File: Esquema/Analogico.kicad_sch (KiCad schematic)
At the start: 33 parts, among them J1 Conex_bat, J2 Conn_01x02, J3 Galga_1, J4 Galga_2, J5 Conn_01x02, P1 USB_C_Plug_USB2.0, U1 REF3020AIDBZT, U2 TMUX154EDGS, U3 TP4057, U4 INA826AIDR, U5 INA826AIDR, U6 XL006, U7 TLV75733PDBV, U8 TLV75733PDBV

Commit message: Cambios en el esquematico del viernes
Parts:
- removed D2: D_Schottky, symbol Device:D_Schottky
- added C4: 47u, Capacitor_SMD:C_0805_2012Metric, symbol Device:C
- added D3: 1N5822, Diode_THT:D_DO-201AD_P15.24mm_Horizontal, symbol Diode:1N5822
- C3: value C -> 220u; footprint (none) -> Capacitor_SMD:C_1206_3216Metric
- C3: value C -> 220u
- L1, L2: value L -> 33u; footprint (none) -> Inductor_SMD:L_APV_APH0630; JLC (none) -> C5349704
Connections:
- net GND: now also C4.2
- net at C3.1, D1.1 (K), P1.A4 (VBUS)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: now also D3.1 (K)
- net at J2.2 (Pin_2), L1.1, U6.2 (EN)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: now also C4.1
- net at C3.2, L2.2: now also D3.2 (A)
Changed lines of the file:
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@@
 		)
 	)
-	(text_box "Mirar datasheet para ver valores"
-		(exclude_from_sim no)
-		(at 17.78 17.78 0)
-		(size 104.14 41.91)
-		(margins 0.9525 0.9525 0.9525 0.9525)
-		(stroke
-			(width 0)
-			(type solid)
-		)
-		(fill
-			(type none)
-		)
-		(effects
-			(font
-				(size 1.27 1.27)
-			)
-			(justify left top)
-		)
-	)
 	(text_box "Mirar datasheet del peso\n"
 		(exclude_from_sim no)
@@
 		(color 0 0 0 0)
 	)
+	(junction
+		(at 39.37 31.75)
+		(diameter 0)
+		(color 0 0 0 0)
+	)
 	(no_connect
 		(at 68.58 66.04)
@@
 	(wire
 		(pts
-			(xy 34.29 31.75) (xy 43.18 31.75)
+			(xy 34.29 31.75) (xy 39.37 31.75)
 		)
 		(stroke
@@
 	(wire
 		(pts
+			(xy 39.37 31.75) (xy 43.18 31.75)
+		)
+		(stroke
+			(width 0)
+			(type default)
+		)
+	)
+	(wire
+		(pts
 			(xy 160.02 48.26) (xy 166.37 48.26)
 		)
@@
 			)
 		)
-		(property "Value" "L"
+		(property "Value" "33u"
 			(at 54.61 22.86 90)
 			(effects
@@
 			)
 		)
-		(property "Footprint" ""
+		(property "Footprint" "Inductor_SMD:L_APV_APH0630"
 			(at 54.61 25.4 0)
 			(effects
@@
 			)
 		)
+		(property "JLC" "C5349704"
+			(at 54.61 25.4 90)
+			(effects
+				(font
+					(size 1.27 1.27)
+				)
+				(hide yes)
+			)
+		)
 		(pin "1"
 		)
@@
 	)
 	(symbol
+		(lib_id "Diode:1N5822")
+		(at 87.63 31.75 180)
+		(unit 1)
+		(exclude_from_sim no)
+		(in_bom yes)
+		(on_board yes)
+		(dnp no)
+		(fields_autoplaced yes)
+		(property "Reference" "D3"
+			(at 87.9475 25.4 0)
+			(effects
+				(font
+					(size 1.27 1.27)
+				)
+			)
+		)
+		(property "Value" "1N5822"
+			(at 87.9475 27.94 0)
+			(effects
+				(font
+					(size 1.27 1.27)
+				)
+			)
+		)
+		(property "Footprint" "Diode_THT:D_DO-201AD_P15.24mm_Horizontal"
+			(at 87.63 27.305 0)
+			(effects
+				(font
+					(size 1.27 1.27)
+				)
+				(hide yes)
+			)
+		)
+		(property "Datasheet" "http://www.vishay.com/docs/88526/1n5820.pdf"
+			(at 87.63 31.75 0)
+			(effects
+				(font
+					(size 1.27 1.27)
+				)
+				(hide yes)
+			)
+		)
+		(property "Description" "40V 3A Schottky Barrier Rectifier Diode, DO-201AD"
+			(at 87.63 31.75 0)
+			(effects
+				(font
+					(size 1.27 1.27)
+				)
+				(hide yes)
+			)
+		)
+		(property "JLC" "C2476"
+			(at 87.63 31.75 0)
+			(effects
+				(font
+					(size 1.27 1.27)
+				)
+				(hide yes)
+			)
+		)
+		(pin "2"
+		)
+		(pin "1"
+		)
+		(instances
+			(project ""
+				(path "/c0191433-e910-4547-8328-ff407e20805d"
+					(reference "D3")
+					(unit 1)
+				)
+			)
+		)
+	)
+	(symbol
 		(lib_id "Device:C")
 		(at 110.49 35.56 0)
@@
 			)
 		)
-		(property "Value" "C"
+		(property "Value" "220u"
 			(at 114.3 36.8299 0)
 			(effects
@@
 			)
 		)
-		(property "Footprint" ""
+		(property "Footprint" "Capacitor_SMD:C_1206_3216Metric"
 			(at 111.4552 39.37 0)
 			(effects
@@
 	)
 	(symbol
-		(lib_id "Device:D_Schottky")
-		(at 87.63 31.75 180)
-		(unit 1)
-		(exclude_from_sim no)
-		(in_bom yes)
-		(on_board yes)
-		(dnp no)
-		(fields_autoplaced yes)
-		(property "Reference" "D2"
-			(at 87.9475 25.4 0)
-			(effects
-				(font
-					(size 1.27 1.27)
-				)
-			)
-		)
-		(property "Value" "D_Schottky"
-			(at 87.9475 27.94 0)
-			(effects
-				(font
-					(size 1.27 1.27)
-				)
-			)
-		)
-		(property "Footprint" ""
-			(at 87.63 31.75 0)
-			(effects
-				(font
-					(size 1.27 1.27)
-				)
-				(hide yes)
-			)
-		)
-		(property "Datasheet" "~"
-			(at 87.63 31.75 0)
-			(effects
-				(font
-					(size 1.27 1.27)
-				)
-				(hide yes)
-			)
-		)
-		(property "Description" "Schottky diode"
-			(at 87.63 31.75 0)
-			(effects
-				(font
-					(size 1.27 1.27)
-				)
-				(hide yes)
-			)
-		)
-		(pin "1"
-		)
-		(pin "2"
-		)
-		(instances
-			(project "Analogico"
-				(path "/c0191433-e910-4547-8328-ff407e20805d"
-					(reference "D2")
-					(unit 1)
-				)
-			)
-		)
-	)
-	(symbol
 		(lib_id "power:GND")
 		(at 179.07 43.18 90)
@@
 			)
 		)
-		(property "Value" "C"
+		(property "Value" "220u"
 			(at 73.66 26.67 90)
 			(effects
@@
 	)
 	(symbol
+		(lib_id "Device:C")
+		(at 39.37 35.56 0)
+		(unit 1)
+		(exclude_from_sim no)
+		(in_bom yes)
+		(on_board yes)
+		(dnp no)
+		(property "Reference" "C4"
+			(at 43.18 34.2899 0)
+			(effects
+				(font
+					(size 1.27 1.27)
+				)
+				(justify left)
+			)
+		)
+		(property "Value" "47u"
+			(at 41.656 39.116 0)
+			(effects
+				(font
+					(size 1.27 1.27)
+				)
+				(justify left)
+			)
+		)
+		(property "Footprint" "Capacitor_SMD:C_0805_2012Metric"
+			(at 40.3352 39.37 0)
+			(effects
+				(font
+					(size 1.27 1.27)
+				)
+				(hide yes)
+			)
+		)
+		(property "Datasheet" "~"
+			(at 39.37 35.56 0)
+			(effects
+				(font
+					(size 1.27 1.27)
+				)
+				(hide yes)
+			)
+		)
+		(property "Description" "Unpolarized capacitor"
+			(at 39.37 35.56 0)
+			(effects
+				(font
+					(size 1.27 1.27)
+				)
+				(hide yes)
+			)
+		)
+		(property "JLC" "C16780"
+			(at 39.37 35.56 0)
+			(effects
+				(font
+					(size 1.27 1.27)
+				)
+				(hide yes)
+			)
+		)
+		(pin "1"
+		)
+		(pin "2"
+		)
+		(instances
+			(project "Analogico"
+				(path "/c0191433-e910-4547-8328-ff407e20805d"
+					(reference "C4")
+					(unit 1)
+				)
+			)
+		)
+	)
+	(symbol
+		(lib_id "power:GND")
+		(at 39.37 39.37 0)
+		(unit 1)
+		(exclude_from_sim no)
+		(in_bom yes)
+		(on_board yes)
+		(dnp no)
+		(fields_autoplaced yes)
+		(property "Reference" "#PWR024"
+			(at 39.37 45.72 0)
+			(effects
+				(font
+					(size 1.27 1.27)
+				)
+				(hide yes)
+			)
+		)
+		(property "Value" "GND"
+			(at 39.37 44.45 0)
+			(effects
+				(font
+					(size 1.27 1.27)
+				)
+			)
+		)
+		(property "Footprint" ""
+			(at 39.37 39.37 0)
+			(effects
+				(font
+					(size 1.27 1.27)
+				)
+				(hide yes)
+			)
+		)
+		(property "Datasheet" ""
+			(at 39.37 39.37 0)
+			(effects
+				(font
+					(size 1.27 1.27)
+				)
+				(hide yes)
+			)
+		)
+		(property "Description" "Power symbol creates a global label with name \"GND\" , ground"
+			(at 39.37 39.37 0)
+			(effects
+				(font
+					(size 1.27 1.27)
+				)
+				(hide yes)
+			)
+		)
+		(pin "1"
+		)
+		(instances
+			(project "Analogico"
+				(path "/c0191433-e910-4547-8328-ff407e20805d"
+					(reference "#PWR024")
+					(unit 1)
+				)
+			)
+		)
+	)
+	(symbol
 		(lib_id "libreria_proy:XL6008")
 		(at 54.61 34.29 0)
@@
 			)
 		)
-		(property "Value" "L"
+		(property "Value" "33u"
 			(at 82.55 39.3699 0)
 			(effects
@@
 			)
 		)
-		(property "Footprint" ""
+		(property "Footprint" "Inductor_SMD:L_APV_APH0630"
 			(at 81.28 38.1 0)
 			(effects
@@
 			(at 81.28 38.1 0)
 			(effects
+				(font
+					(size 1.27 1.27)
+				)
+				(hide yes)
+			)
+		)
+		(property "JLC" "C5349704"
+			(at 81.28 38.1 0)
+			(effects

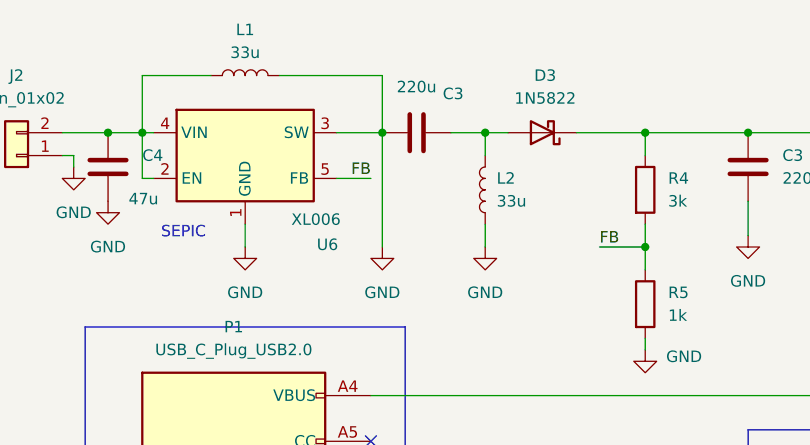
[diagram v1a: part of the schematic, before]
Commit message: He añadido los correspondientes datasheets y he corregido un componente que estaba mal colocado.
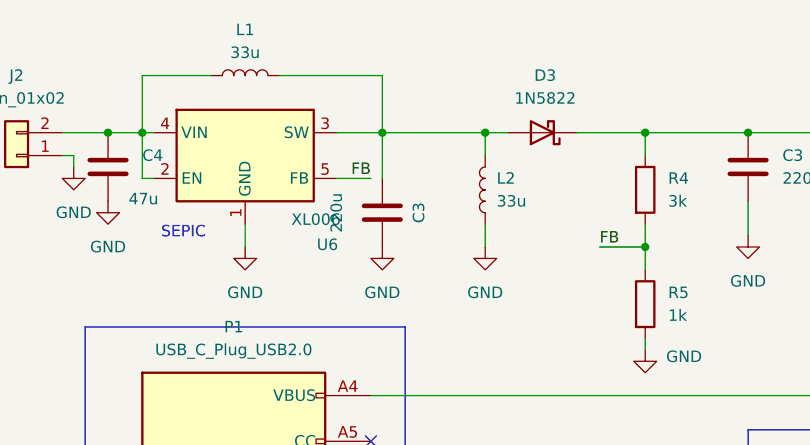
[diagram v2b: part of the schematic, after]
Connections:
- net GND: no longer L1.2, U6.3 (SW)
- net at C3.2, D3.2 (A), L2.2: now also L1.2, U6.3 (SW)
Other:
- moved on the sheet: C3
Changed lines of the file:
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@@
 	)
 	(junction
-		(at 125.73 60.96)
+		(at 69.85 31.75)
 		(diameter 0)
 		(color 0 0 0 0)
 	)
 	(junction
-		(at 69.85 31.75)
+		(at 125.73 60.96)
 		(diameter 0)
 		(color 0 0 0 0)
@@
 	(wire
 		(pts
-			(xy 69.85 44.45) (xy 69.85 31.75)
+			(xy 166.37 71.12) (xy 185.42 71.12)
 		)
 		(stroke
@@
 	(wire
 		(pts
-			(xy 166.37 71.12) (xy 185.42 71.12)
+			(xy 99.06 44.45) (xy 99.06 46.99)
 		)
 		(stroke
@@
 	(wire
 		(pts
-			(xy 99.06 44.45) (xy 99.06 46.99)
+			(xy 76.2 137.16) (xy 78.74 137.16)
 		)
 		(stroke
@@
 	(wire
 		(pts
-			(xy 76.2 137.16) (xy 78.74 137.16)
+			(xy 69.85 31.75) (xy 69.85 36.83)
 		)
 		(stroke
@@
 	(wire
 		(pts
+			(xy 69.85 31.75) (xy 81.28 31.75)
+		)
+		(stroke
+			(width 0)
+			(type default)
+		)
+	)
+	(wire
+		(pts
 			(xy 87.63 144.78) (xy 87.63 137.16)
 		)
@@
 	(wire
 		(pts
-			(xy 77.47 31.75) (xy 81.28 31.75)
-		)
-		(stroke
-			(width 0)
-			(type default)
-		)
-	)
-	(wire
-		(pts
 			(xy 248.92 92.71) (xy 248.92 93.98)
 		)
@@
 			)
 		)
-		(property "Datasheet" "~"
+		(property "Datasheet" "https://www.lcsc.com/datasheet/C5349704.pdf"
 			(at 54.61 25.4 0)
 			(effects
@@
 	(symbol
 		(lib_id "Device:C")
-		(at 73.66 31.75 90)
+		(at 69.85 40.64 180)
 		(unit 1)
 		(exclude_from_sim no)
@@
 		(dnp no)
 		(property "Reference" "C3"
-			(at 77.724 27.432 90)
+			(at 73.914 40.64 90)
 			(effects
 				(font
@@
 		)
 		(property "Value" "220u"
-			(at 73.66 26.67 90)
+			(at 64.77 40.64 90)
 			(effects
 				(font
@@
 		)
 		(property "Footprint" ""
-			(at 77.47 30.7848 0)
+			(at 68.8848 36.83 0)
 			(effects
 				(font
@@
 		)
 		(property "Datasheet" "~"
-			(at 73.66 31.75 0)
+			(at 69.85 40.64 0)
 			(effects
 				(font
@@
 		)
 		(property "Description" "Unpolarized capacitor"
-			(at 73.66 31.75 0)
+			(at 69.85 40.64 0)
 			(effects
 				(font
@@
 			)
 		)
-		(property "Datasheet" "~"
+		(property "Datasheet" "https://www.lcsc.com/datasheet/C5349704.pdf"
 			(at 81.28 38.1 0)
 			(effects

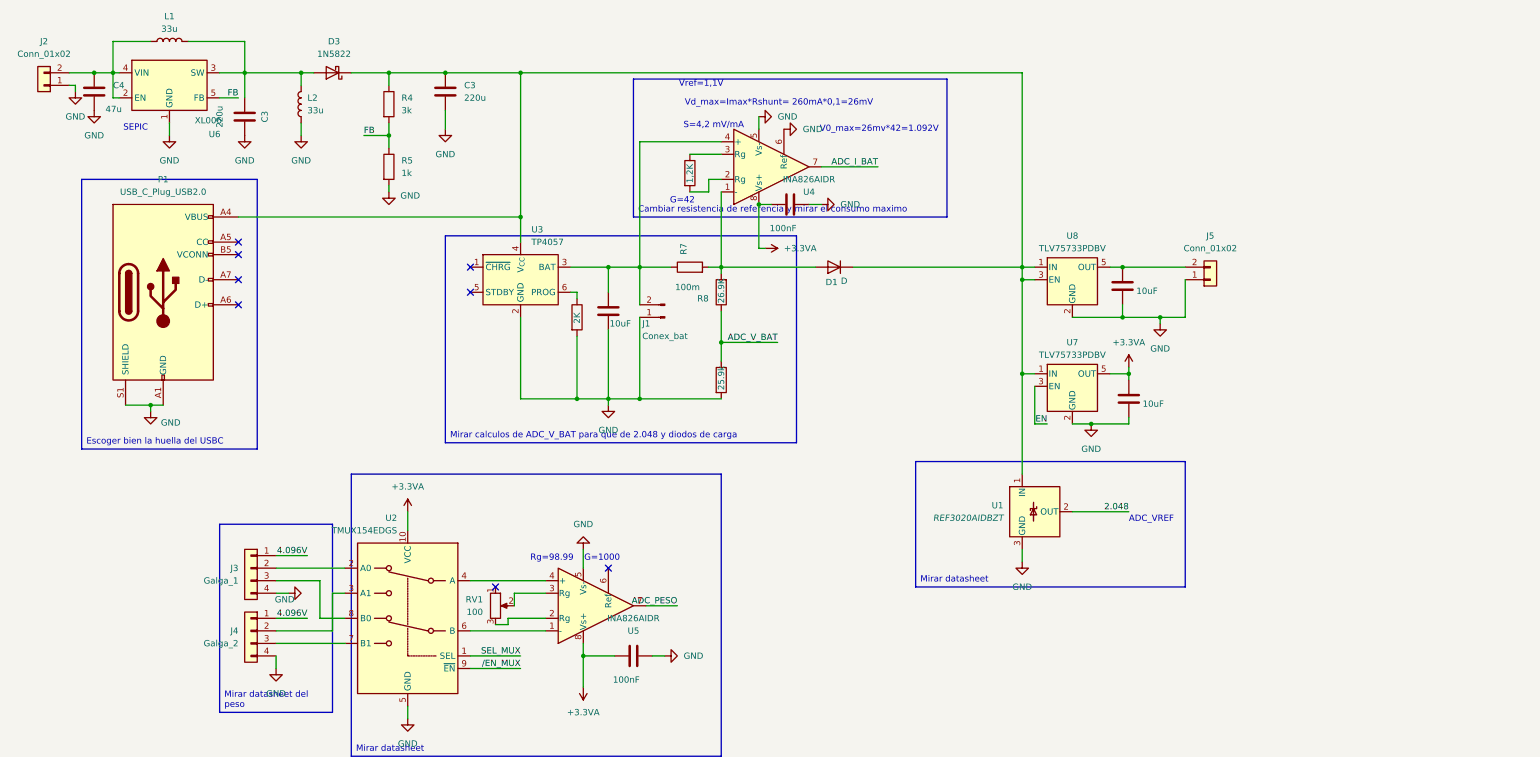
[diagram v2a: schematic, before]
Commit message: He añadido la footprint y simbolo del stm32f429zi
Signed-off-by: ricardo.socorro <ricardo.socorro@alumnos.upm.es>
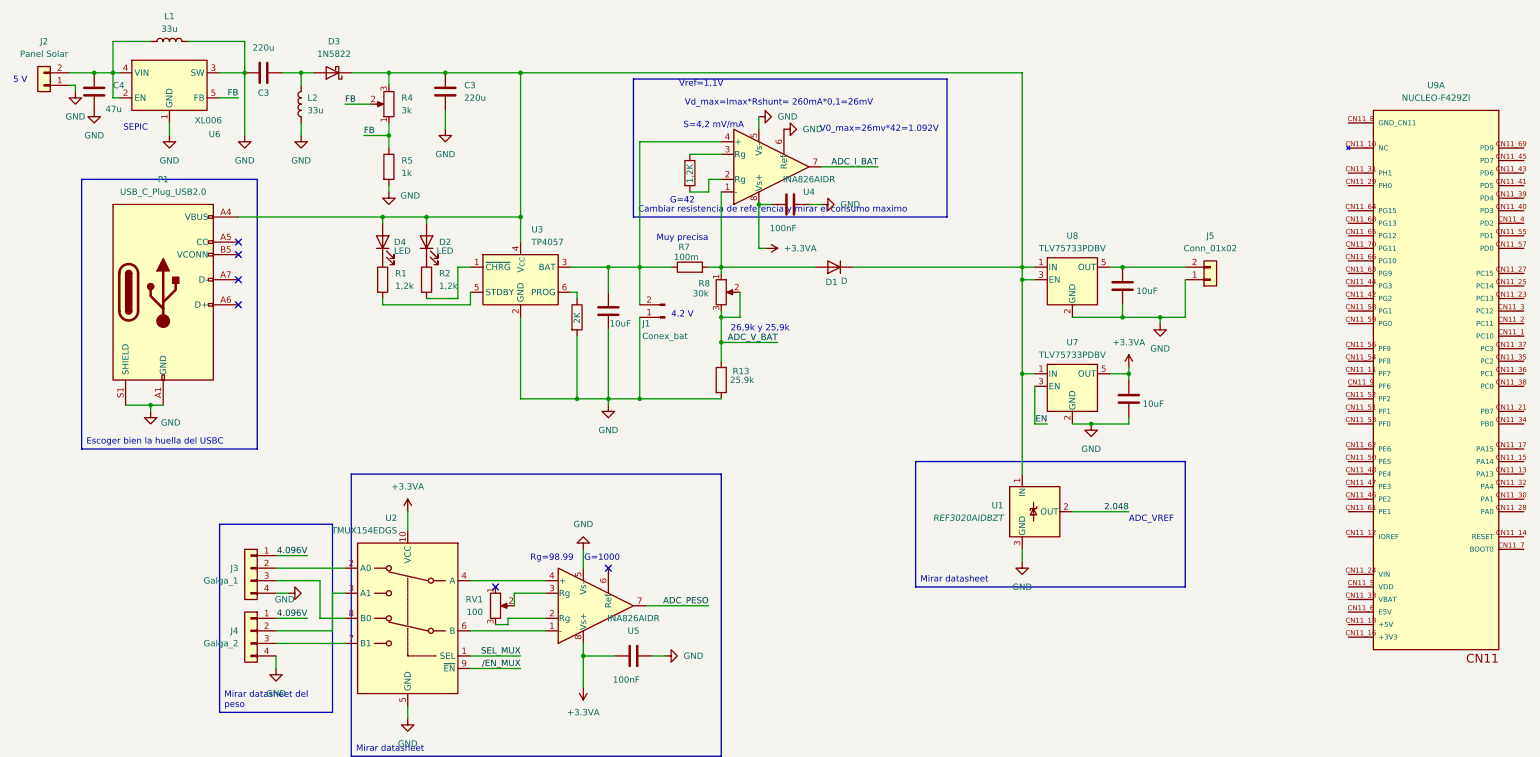
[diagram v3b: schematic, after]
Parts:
- removed R4: 3k, symbol Device:R
- removed R8: 26.9K, Resistor_SMD:R_0603_1608Metric, symbol Device:R
- added D2, D4: LED, symbol Device:LED
- added R1, R2: 1,2k, symbol Device:R
- added R4: 3k, symbol Device:R_Potentiometer
- added R8: 30k, symbol Device:R_Potentiometer
- added U9: NUCLEO-F429ZI, stm32f429zi_symbol_footprint:MODULE_NUCLEO-F429ZI, symbol NUCLEO-F429ZI:NUCLEO-F429ZI
- J2: value Conn_01x02 -> Panel Solar
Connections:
- net ADC_V_BAT: now also R8.2, R8.3
- net FB: now also R4.1, R4.2
- net GND: now also L1.2, U6.3 (SW)
- net at D1.2 (A), R7.2, U4.1 (-): now also R8.1
- net at C3.1, D1.1 (K), D3.1 (K)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: now also D2.2 (A), D4.2 (A), R4.3
- net at C3.2, D3.2 (A), L2.2: no longer L1.2, U6.3 (SW)
- net at U3.1 (~{CHRG}): now also R2.2
- net at U3.5 (STDBY): now also R1.2
- new net: D2.1 (K), R2.1
- new net: D4.1 (K), R1.1
- new net: U9.CN11_10 (NC), U9.CN11_26 (NC), U9.CN11_67 (NC)
- new net GND_CN11: U9.CN11_19 (GND_CN11), U9.CN11_20 (GND_CN11), U9.CN11_22 (GND_CN11), U9.CN11_49 (GND_CN11), U9.CN11_60 (GND_CN11), U9.CN11_71 (GND_CN11), U9.CN11_72 (GND_CN11), U9.CN11_8 (GND_CN11)
- no-connect marks 8 -> 6
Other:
- note added: "26,9k y 25,9k"
- note added: "4.2 V"
- note added: "5 V"
- note added: "Muy precisa"
- moved on the sheet: C3

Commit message: Huellas y componentes ya asignados
Signed-off-by: ricardo.socorro <ricardo.socorro@alumnos.upm.es>
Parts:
- added C6: 470nF, Capacitor_SMD:C_0805_2012Metric, symbol Device:C
- added R3: 1.5k, Resistor_SMD:R_0805_2012Metric, symbol Device:R
- added R9: 26.1k, Resistor_SMD:R_0805_2012Metric, symbol Device:R
- C10: renamed from C3; value 220u -> 220uF; footprint (none) -> Capacitor_SMD:C_1206_3216Metric; JLC (none) -> C412252
- C4: value 47u -> 47uF
- C9: renamed from C3; value 220u -> 220uF; JLC (none) -> C412252
- D2, D4: footprint (none) -> LED_THT:LED_D3.0mm; JLC (none) -> C85161
- J1: footprint (none) -> Connector_JST:JST_PH_S2B-PH-K_1x02_P2.00mm_Horizontal
- J2, J3, J4, J5: footprint (none) -> TerminalBlock_4Ucon:TerminalBlock_4Ucon_1x02_P3.50mm_Horizontal; JLC (none) -> C695629
- P1: footprint (none) -> Connector_USB:USB_C_Plug_ShenzhenJingTuoJin_918-118A2021Y40002_Vertical
- R1, R2: footprint (none) -> Resistor_SMD:R_0805_2012Metric; JLC (none) -> C114526
- R13: value 25.9k -> 25.5k
- R4: value 3k -> 2k; footprint (none) -> Potentiometer_THT:Potentiometer_Bourns_3266Y_Vertical; JLC (none) -> C48997938
- R5: footprint (none) -> Resistor_SMD:R_0805_2012Metric
- R8: value 30k -> 1k; footprint (none) -> Potentiometer_THT:Potentiometer_Bourns_3266Y_Vertical; JLC (none) -> C48997938
- RV1: footprint (none) -> Potentiometer_THT:Potentiometer_Bourns_3266Y_Vertical; JLC (none) -> C48997939
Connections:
- net FB: now also R3.2; no longer R4.1, R4.2
- net GND: now also C6.2
- net at D1.2 (A), R7.2, U4.1 (-): now also R9.1; no longer R8.1
- net at C9.1, D1.1 (K), D2.2 (A)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: now also R4.2, C6.1
- new net: R3.1, R4.1
- new net: R8.1, R9.2
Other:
- note added: "26,9k y 25,9k y 1%"
- note added: "3k y 1k"
- note added: "No existe 25.9k Usamos 25.5k y la de arriba tiene que ser menos de 26.5k"
- note removed: "26,9k y 25,9k"
- moved on the sheet: R13, R4, R5, R8, U9A

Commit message: PCB 1.0
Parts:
- removed J5: Conn_01x02, TerminalBlock_4Ucon:TerminalBlock_4Ucon_1x02_P3.50mm_Horizontal, symbol Connector_Generic:Conn_01x02
- removed U2: TMUX154EDGS, Package_SO:VSSOP-10_3x3mm_P0.5mm, symbol Analog_Switch:TMUX154EDGS
- removed U9: NUCLEO-F429ZI, stm32f429zi_symbol_footprint:MODULE_NUCLEO-F429ZI, symbol NUCLEO-F429ZI:NUCLEO-F429ZI
- added C3: 100nF, Capacitor_SMD:C_0805_2012Metric, symbol Device:C
- added RV2: 100, Potentiometer_THT:Potentiometer_Bourns_3266Y_Vertical, symbol Device:R_Potentiometer
- added U10: NUCLEO-F429ZI, mis_footprints:MODULE_NUCLEO-F429ZI_FEMALE, symbol mis_componentes:NUCLEO-F429ZI_FEMALE
- added U2: INA826AIDR, Package_SO:SOIC-8_3.9x4.9mm_P1.27mm, symbol Amplifier_Instrumentation:INA849D
- added U9: NUCLEO-F429ZI, NUCLEO-F429ZI:MODULE_NUCLEO-F429ZI, symbol mis_componentes:NUCLEO-F429ZI
- J3, J4: footprint TerminalBlock_4Ucon:TerminalBlock_4Ucon_1x02_P3.50mm_Horizontal -> TerminalBlock:TerminalBlock_MaiXu_MX126-5.0-04P_1x04_P5.00mm; JLC C695629 -> C192769
- P1: footprint Connector_USB:USB_C_Plug_ShenzhenJingTuoJin_918-118A2021Y40002_Vertical -> Connector_USB:USB_C_Receptacle_GCT_USB4125-xx-x-0190_6P_TopMnt_Horizontal
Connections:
- net 4.096V is gone; now on net 2.048: J3.1 (Pin_1), J4.1 (Pin_1)
- net +3.3VA: now also C3.1, U2.8 (Vs+)
- net 2.048: now also U10.CN10_1 (AVDD_CN10), U10.CN7_6 (AREF), U9.CN10_1 (AVDD_CN10)
- net ADC_I_BAT: now also U10.CN9_5 (A2/ADC123_IN13)
- net EN: now also U10.CN7_20 (D8/IO)
- net GND: now also C3.2, U10.CN10_17 (GND_CN10), U10.CN10_22 (GND_CN10), U10.CN10_27 (GND_CN10), U10.CN10_3 (AGND_CN10), U10.CN10_5 (GND_CN10), U10.CN7_8 (GND_CN7), U10.CN8_11 (GND_CN8), U10.CN8_13 (GND_CN8), U10.CN9_12 (GND_CN9), U10.CN9_23 (GND_CN9), U2.5 (Vs-), U9.CN10_17 (GND_CN10), U9.CN10_22 (GND_CN10), U9.CN10_27 (GND_CN10), U9.CN10_3 (AGND_CN10), U9.CN10_5 (GND_CN10)
- net at J4.2 (Pin_2): now also U2.4 (+)
- net at J4.3 (Pin_3): now also U2.1 (-)
- net at J3.2 (Pin_2): now also U5.4 (+)
- net at U5.1 (-): now also J3.3 (Pin_3)
- net +3.3V: now reaches C5.1, U8.5 (OUT)
- net +3.3V: now also U10.CN8_7 (+3V3_CN8)
- net ADC_PESO renamed ADC_PESO_1
- net ADC_PESO_1: now also U10.CN9_1 (A0/ADC123_IN3)
- new net: RV2.3, U2.2 (Rg)
- new net: RV2.2, U2.3 (Rg)
- new net ADC_PESO_2: U10.CN9_3 (A1/ADC123_IN10), U2.7
- no-connect marks 6 -> 120
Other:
- moved on the sheet: J3, J4

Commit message: PCB ver. 1.1 Signed-off-by: ricardo.socorro <ricardo.socorro@alumnos.upm.es>
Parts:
- removed U9: NUCLEO-F429ZI, NUCLEO-F429ZI:MODULE_NUCLEO-F429ZI, symbol mis_componentes:NUCLEO-F429ZI
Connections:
- net ADC_V_BAT: now also U10.CN10_7 (A6/ADC_A_IN)
- net EN: now also U10.CN10_13 (D26/IO); no longer U10.CN7_20 (D8/IO)
- no-connect marks 120 -> 91
